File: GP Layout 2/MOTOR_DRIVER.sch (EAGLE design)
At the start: 52 parts, among them U3 MIC4604YM, U6 MIC4604YM, U7 ATMEGA328P_TQFP, Y1 16MHz

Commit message: checking that its updated
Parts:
- renumbered BOT_REVERSE to BOT_REV, TOP_REVERSE to TOP_REV, U3 to GATE1, U6 to GATE2
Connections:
- net BLT_RX: now also U$1.8; no longer U$1.7
- net BLT_TX: now also U$1.7; no longer U$1.8
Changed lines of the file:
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@@
 <parts>
 <part name="TOP_FWD" library="CSD18502KCS" deviceset="CSD18502KCS_KCS_3" device=""/>
-<part name="BOT_REVERSE" library="CSD18502KCS" deviceset="CSD18502KCS_KCS_3" device=""/>
+<part name="BOT_REV" library="CSD18502KCS" deviceset="CSD18502KCS_KCS_3" device=""/>
 <part name="FRAME1" library="frames" deviceset="A3L-LOC" device=""/>
-<part name="U3" library="MIC4604" deviceset="MIC4604YM" device=""/>
+<part name="GATE1" library="MIC4604" deviceset="MIC4604YM" device=""/>
 <part name="C1" library="resistor" deviceset="C-US" device="025-050X050" value="10uF"/>
 <part name="C2" library="resistor" deviceset="C-US" device="025-050X050" value="10uF"/>
 <part name="LSP3" library="solpad" deviceset="SE14" device=""/>
-<part name="TOP_REVERSE" library="CSD18502KCS" deviceset="CSD18502KCS_KCS_3" device=""/>
+<part name="TOP_REV" library="CSD18502KCS" deviceset="CSD18502KCS_KCS_3" device=""/>
 <part name="BOT_FWD" library="CSD18502KCS" deviceset="CSD18502KCS_KCS_3" device=""/>
-<part name="U6" library="MIC4604" deviceset="MIC4604YM" device=""/>
+<part name="GATE2" library="MIC4604" deviceset="MIC4604YM" device=""/>
 <part name="C3" library="resistor" deviceset="C-US" device="025-050X050" value="10uF"/>
 <part name="C4" library="resistor" deviceset="C-US" device="025-050X050" value="10uF"/>
@@
 <instances>
 <instance part="TOP_FWD" gate="A" x="124.46" y="210.82" rot="MR270"/>
-<instance part="BOT_REVERSE" gate="A" x="124.46" y="114.3" rot="MR270"/>
+<instance part="BOT_REV" gate="A" x="124.46" y="114.3" rot="MR270"/>
 <instance part="FRAME1" gate="G$1" x="0" y="0"/>
-<instance part="U3" gate="A" x="86.36" y="142.24" rot="MR0"/>
+<instance part="GATE1" gate="A" x="86.36" y="142.24" rot="MR0"/>
 <instance part="C1" gate="G$1" x="106.68" y="132.08" rot="R180"/>
 <instance part="C2" gate="G$1" x="116.84" y="132.08" rot="R180"/>
 <instance part="LSP3" gate="1" x="142.24" y="132.08" rot="R270"/>
-<instance part="TOP_REVERSE" gate="A" x="243.84" y="213.36" rot="R270"/>
+<instance part="TOP_REV" gate="A" x="243.84" y="213.36" rot="R270"/>
 <instance part="BOT_FWD" gate="A" x="243.84" y="114.3" rot="R270"/>
-<instance part="U6" gate="A" x="281.94" y="142.24"/>
+<instance part="GATE2" gate="A" x="281.94" y="142.24"/>
 <instance part="C3" gate="G$1" x="261.62" y="132.08" rot="MR180"/>
 <instance part="C4" gate="G$1" x="251.46" y="132.08" rot="MR180"/>
@@
 <net name="N$2" class="0">
 <segment>
-<pinref part="U3" gate="A" pin="LO"/>
+<pinref part="GATE1" gate="A" pin="LO"/>
 <wire x1="30.48" y1="142.24" x2="15.24" y2="142.24" width="0.1524" layer="91"/>
 <wire x1="15.24" y1="142.24" x2="15.24" y2="119.38" width="0.1524" layer="91"/>
-<pinref part="BOT_REVERSE" gate="A" pin="GATE"/>
+<pinref part="BOT_REV" gate="A" pin="GATE"/>
 <wire x1="15.24" y1="119.38" x2="124.46" y2="119.38" width="0.1524" layer="91"/>
 <wire x1="124.46" y1="119.38" x2="124.46" y2="114.3" width="0.1524" layer="91"/>
@@
 <wire x1="124.46" y1="218.44" x2="88.9" y2="218.44" width="0.1524" layer="91"/>
 <wire x1="88.9" y1="218.44" x2="88.9" y2="137.16" width="0.1524" layer="91"/>
-<pinref part="U3" gate="A" pin="HO"/>
+<pinref part="GATE1" gate="A" pin="HO"/>
 <wire x1="88.9" y1="137.16" x2="86.36" y2="137.16" width="0.1524" layer="91"/>
 </segment>
@@
 <net name="N$4" class="0">
 <segment>
-<pinref part="U3" gate="A" pin="HS"/>
+<pinref part="GATE1" gate="A" pin="HS"/>
 <wire x1="86.36" y1="134.62" x2="88.9" y2="134.62" width="0.1524" layer="91"/>
 <wire x1="88.9" y1="134.62" x2="88.9" y2="124.46" width="0.1524" layer="91"/>
@@
 <net name="N$5" class="0">
 <segment>
-<pinref part="U3" gate="A" pin="HB"/>
+<pinref part="GATE1" gate="A" pin="HB"/>
 <pinref part="C2" gate="G$1" pin="2"/>
 <wire x1="86.36" y1="139.7" x2="106.68" y2="139.7" width="0.1524" layer="91"/>
@@
 <net name="N$9" class="0">
 <segment>
-<pinref part="U6" gate="A" pin="LO"/>
+<pinref part="GATE2" gate="A" pin="LO"/>
 <wire x1="337.82" y1="142.24" x2="353.06" y2="142.24" width="0.1524" layer="91"/>
 <wire x1="353.06" y1="142.24" x2="353.06" y2="119.38" width="0.1524" layer="91"/>
@@
 <net name="N$10" class="0">
 <segment>
-<pinref part="TOP_REVERSE" gate="A" pin="GATE"/>
+<pinref part="TOP_REV" gate="A" pin="GATE"/>
 <wire x1="243.84" y1="213.36" x2="243.84" y2="218.44" width="0.1524" layer="91"/>
 <wire x1="243.84" y1="218.44" x2="279.4" y2="218.44" width="0.1524" layer="91"/>
 <wire x1="279.4" y1="218.44" x2="279.4" y2="137.16" width="0.1524" layer="91"/>
-<pinref part="U6" gate="A" pin="HO"/>
+<pinref part="GATE2" gate="A" pin="HO"/>
 <wire x1="279.4" y1="137.16" x2="281.94" y2="137.16" width="0.1524" layer="91"/>
 </segment>
@@
 <net name="N$11" class="0">
 <segment>
-<pinref part="U6" gate="A" pin="HS"/>
+<pinref part="GATE2" gate="A" pin="HS"/>
 <wire x1="281.94" y1="134.62" x2="279.4" y2="134.62" width="0.1524" layer="91"/>
 <wire x1="279.4" y1="134.62" x2="279.4" y2="124.46" width="0.1524" layer="91"/>
@@
 <net name="N$12" class="0">
 <segment>
-<pinref part="U6" gate="A" pin="HB"/>
+<pinref part="GATE2" gate="A" pin="HB"/>
 <pinref part="C4" gate="G$1" pin="2"/>
 <wire x1="281.94" y1="139.7" x2="261.62" y2="139.7" width="0.1524" layer="91"/>
@@
 <net name="LI2_TOP" class="0">
 <segment>
-<pinref part="U6" gate="A" pin="HI"/>
+<pinref part="GATE2" gate="A" pin="HI"/>
 <wire x1="337.82" y1="134.62" x2="350.52" y2="134.62" width="0.1524" layer="91"/>
 <label x="342.9" y="134.62" size="1.778" layer="95"/>
@@
 <net name="HI2_TOP" class="0">
 <segment>
-<pinref part="U6" gate="A" pin="LI"/>
+<pinref part="GATE2" gate="A" pin="LI"/>
 <wire x1="337.82" y1="137.16" x2="350.52" y2="137.16" width="0.1524" layer="91"/>
 <label x="342.9" y="137.16" size="1.778" layer="95"/>
@@
 <net name="GND_TOP" class="0">
 <segment>
-<pinref part="BOT_REVERSE" gate="A" pin="SOURCE"/>
+<pinref part="BOT_REV" gate="A" pin="SOURCE"/>
 <wire x1="127" y1="48.26" x2="127" y2="40.64" width="0.1524" layer="91"/>
-<pinref part="U3" gate="A" pin="VSS"/>
+<pinref part="GATE1" gate="A" pin="VSS"/>
 <wire x1="30.48" y1="139.7" x2="12.7" y2="139.7" width="0.1524" layer="91"/>
 <wire x1="12.7" y1="139.7" x2="12.7" y2="40.64" width="0.1524" layer="91"/>
@@
 <pinref part="BOT_FWD" gate="A" pin="SOURCE"/>
 <wire x1="241.3" y1="48.26" x2="241.3" y2="40.64" width="0.1524" layer="91"/>
-<pinref part="U6" gate="A" pin="VSS"/>
+<pinref part="GATE2" gate="A" pin="VSS"/>
 <wire x1="337.82" y1="139.7" x2="355.6" y2="139.7" width="0.1524" layer="91"/>
 <wire x1="355.6" y1="139.7" x2="355.6" y2="40.64" width="0.1524" layer="91"/>
@@
 <wire x1="86.36" y1="220.98" x2="86.36" y2="147.32" width="0.1524" layer="91"/>
 <junction x="127" y="220.98"/>
-<pinref part="U3" gate="A" pin="VDD"/>
-<pinref part="TOP_REVERSE" gate="A" pin="DRAIN"/>
+<pinref part="GATE1" gate="A" pin="VDD"/>
+<pinref part="TOP_REV" gate="A" pin="DRAIN"/>
 <wire x1="86.36" y1="147.32" x2="86.36" y2="142.24" width="0.1524" layer="91"/>
 <wire x1="241.3" y1="220.98" x2="241.3" y2="213.36" width="0.1524" layer="91"/>
 <wire x1="241.3" y1="220.98" x2="281.94" y2="220.98" width="0.1524" layer="91"/>
 <wire x1="281.94" y1="220.98" x2="281.94" y2="147.32" width="0.1524" layer="91"/>
-<pinref part="U6" gate="A" pin="VDD"/>
+<pinref part="GATE2" gate="A" pin="VDD"/>
 <wire x1="281.94" y1="147.32" x2="281.94" y2="142.24" width="0.1524" layer="91"/>
 <wire x1="127" y1="220.98" x2="175.26" y2="220.98" width="0.1524" layer="91"/>
@@
 <segment>
 <pinref part="TOP_FWD" gate="A" pin="SOURCE"/>
-<pinref part="BOT_REVERSE" gate="A" pin="DRAIN"/>
+<pinref part="BOT_REV" gate="A" pin="DRAIN"/>
 <wire x1="127" y1="144.78" x2="127" y2="132.08" width="0.1524" layer="91"/>
 <pinref part="LSP3" gate="1" pin="MP"/>
@@
 <net name="MOTOR_LOW_TOP" class="0">
 <segment>
-<pinref part="TOP_REVERSE" gate="A" pin="SOURCE"/>
+<pinref part="TOP_REV" gate="A" pin="SOURCE"/>
 <pinref part="BOT_FWD" gate="A" pin="DRAIN"/>
 <wire x1="241.3" y1="147.32" x2="241.3" y2="132.08" width="0.1524" layer="91"/>
@@
 <net name="LI1_TOP" class="0">
 <segment>
-<pinref part="U3" gate="A" pin="LI"/>
+<pinref part="GATE1" gate="A" pin="LI"/>
 <wire x1="30.48" y1="137.16" x2="20.32" y2="137.16" width="0.1524" layer="91"/>
 <label x="20.32" y="137.16" size="1.778" layer="95"/>
@@
 <net name="HI1_TOP" class="0">
 <segment>
-<pinref part="U3" gate="A" pin="HI"/>
+<pinref part="GATE1" gate="A" pin="HI"/>
 <wire x1="30.48" y1="134.62" x2="20.32" y2="134.62" width="0.1524" layer="91"/>
 <label x="20.32" y="134.62" size="1.778" layer="95"/>
@@
 </segment>
 </net>
-<net name="BLT_RX" class="0">
+<net name="BLT_TX" class="0">
 <segment>
 <wire x1="238.76" y1="147.32" x2="223.52" y2="147.32" width="0.1524" layer="91"/>
 <label x="223.52" y="147.32" size="1.778" layer="95"/>
 <pinref part="U$1" gate="G$1" pin="7"/>
-</segment>
-</net>
-<net name="BLT_TX" class="0">
-<segment>
-<wire x1="238.76" y1="144.78" x2="223.52" y2="144.78" width="0.1524" layer="91"/>
-<label x="223.52" y="144.78" size="1.778" layer="95"/>
-<pinref part="U$1" gate="G$1" pin="8"/>
 </segment>
 </net>
@@
 </segment>
 </net>
+<net name="BLT_RX" class="0">
+<segment>
+<wire x1="238.76" y1="144.78" x2="223.52" y2="144.78" width="0.1524" layer="91"/>
+<label x="223.52" y="144.78" size="1.778" layer="95"/>
+<pinref part="U$1" gate="G$1" pin="8"/>
+</segment>
+</net>

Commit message: added gpio, modified layout
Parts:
- added MOTOR_NEG_B: SE14, solpad:SE14
- added TGPIO: (no value), con-lsta:FE09-1
- renumbered LSP3 to MOTOR_POS, LSP4 to BATT_HIGH, LSP5 to BATT_LOW, LSP6 to MOTOR_NEG
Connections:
- removed net M1_GPIO4: U7.PD3(INT1)
- new net LED1: U$1.14/A0
- new net LED2: U$1.15/A1
- new net LED3: U$1.16/A2
- new net TGPIO1: TGPIO.1, U$1.33/A14
- new net TGPIO2: TGPIO.2, U$1.34/A15
- new net TGPIO3: TGPIO.3, U$1.35/A16
- new net TGPIO4: TGPIO.4, U$1.36/A17
- new net TGPIO5: TGPIO.5, U$1.37/A18
- new net TGPIO6: TGPIO.6, U$1.38/A19
- new net TGPIO7: TGPIO.7, U$1.39/A20
- new net TGPIO8: TGPIO.8, U$1.A21/DAC0
- new net TGPIO9: TGPIO.9, U$1.A22/DAC1
- net BATT_VOLTAGE_SENSE: now also U$1.17/A3; no longer U$1.14/A0
- net EMF_SENSE_HIGH: now also U$1.19/A5/SCL; no longer U$1.17/A3
- net EMF_SENSE_LOW: now also U$1.18/A4/SDA; no longer U$1.16/A2
- net GND_TOP: now also MOTOR_NEG_B.MP
- net HALL1_B: now also U$1.1/TX; no longer U$1.39/A20
- net HALL2: now also U7.PD3(INT1)
- net HALL2_B: now also U$1.2; no longer U$1.38/A19
- net REC_EXTRA1: now also U$1.22/A8
- net REC_EXTRA2: now also U$1.23/A9
- net REC_MOTOR: now also REC.4, U$1.21/A7; no longer REC.3, U$1.15/A1
- net REC_SERVO: now also REC.3, U$1.20/A6; no longer REC.4, U$1.18/A4/SDA
- net SERVO: now also U$1.9/CS; no longer U$1.20/A6

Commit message: ISCP connectors
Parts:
- removed TXRX: (no value), con-lsta:FE02-1
- added PROGRAM: (no value), arduino_jw:ARDUINO_CONN-ICSP
- R1: value 9090 -> 2800
- R2: value 4750 -> 1620
- R3: value 2.32M -> 2320
- R4: value 1.15M -> 1150
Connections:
- net RX: no longer TXRX.1
- net TX: no longer TXRX.2
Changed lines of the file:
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@@
 <part name="FUSE" library="minifuse" deviceset="FUSEHOLDER3588" device=""/>
 <part name="BIG_SWITCH" library="bigswitch" deviceset="BIGSWITCH" device=""/>
-<part name="R1" library="SparkFun-Resistors" deviceset="0.3OHM" device="-0805-1/8W-1%" value="9090"/>
-<part name="R2" library="SparkFun-Resistors" deviceset="0.3OHM" device="-0805-1/8W-1%" value="4750"/>
+<part name="R1" library="SparkFun-Resistors" deviceset="0.3OHM" device="-0805-1/8W-1%" value="2800"/>
+<part name="R2" library="SparkFun-Resistors" deviceset="0.3OHM" device="-0805-1/8W-1%" value="1620"/>
 <part name="SUPPLY2" library="supply2" deviceset="GND" device=""/>
-<part name="R3" library="SparkFun-Resistors" deviceset="0.3OHM" device="-0805-1/8W-1%" value="2.32M"/>
-<part name="R4" library="SparkFun-Resistors" deviceset="0.3OHM" device="-0805-1/8W-1%" value="1.15M"/>
+<part name="R3" library="SparkFun-Resistors" deviceset="0.3OHM" device="-0805-1/8W-1%" value="2320"/>
+<part name="R4" library="SparkFun-Resistors" deviceset="0.3OHM" device="-0805-1/8W-1%" value="1150"/>
 <part name="U$2" library="heatsink" deviceset="HEATSINK" device=""/>
 <part name="U$4" library="heatsink" deviceset="HEATSINK" device=""/>
@@
 <part name="HALL1_B" library="con-lstb" deviceset="MA03-1" device=""/>
 <part name="HALL2_B" library="con-lstb" deviceset="MA03-1" device=""/>
-<part name="TXRX" library="con-lsta" deviceset="FE02-1" device=""/>
 <part name="MOTOR_NEG_B" library="solpad" deviceset="SE14" device=""/>
 <part name="TGPIO" library="con-lsta" deviceset="FE09-1" device=""/>
+<part name="PROGRAM" library="arduino_jw" deviceset="ARDUINO_CONN-ICSP" device=""/>
 </parts>
 <sheets>
@@
 <instance part="HALL1_B" gate="G$1" x="304.8" y="104.14"/>
 <instance part="HALL2_B" gate="G$1" x="304.8" y="86.36"/>
-<instance part="TXRX" gate="G$1" x="208.28" y="71.12"/>
 <instance part="TGPIO" gate="G$1" x="121.92" y="68.58"/>
+<instance part="PROGRAM" gate="G$1" x="236.22" y="60.96"/>
 </instances>
 <busses>
@@
 </segment>
 </net>
-<net name="TX" class="0">
-<segment>
-<pinref part="TXRX" gate="G$1" pin="2"/>
-<wire x1="215.9" y1="71.12" x2="226.06" y2="71.12" width="0.1524" layer="91"/>
-<label x="220.98" y="71.12" size="1.778" layer="95"/>
-</segment>
-</net>
-<net name="RX" class="0">
-<segment>
-<pinref part="TXRX" gate="G$1" pin="1"/>
-<wire x1="215.9" y1="68.58" x2="226.06" y2="68.58" width="0.1524" layer="91"/>
-<label x="220.98" y="68.58" size="1.778" layer="95"/>
-</segment>
-</net>

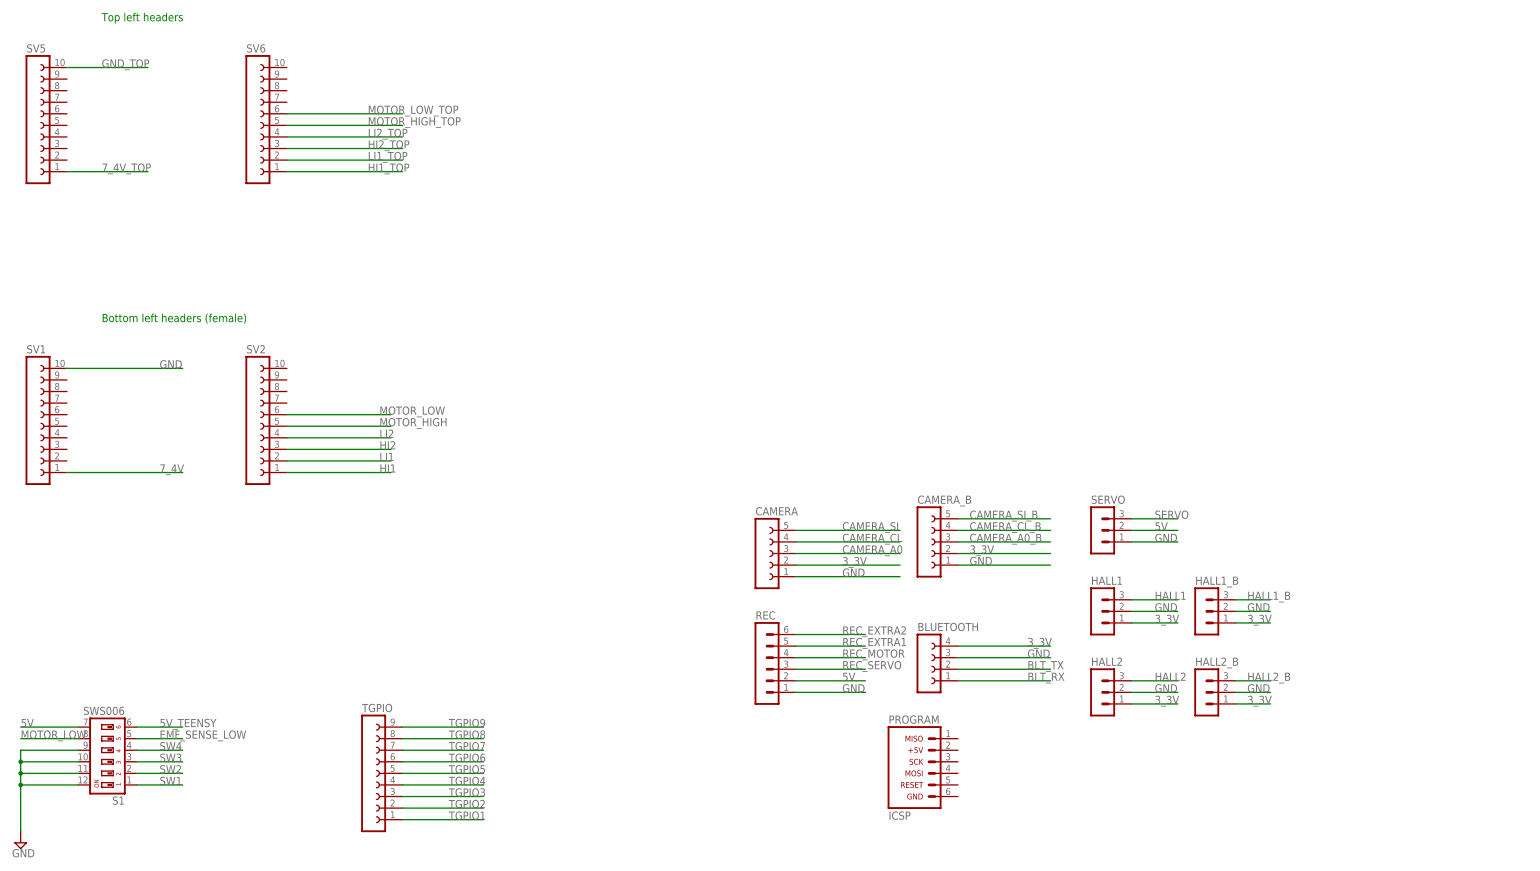
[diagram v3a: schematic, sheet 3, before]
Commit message: added led driver, indicator leds, etc
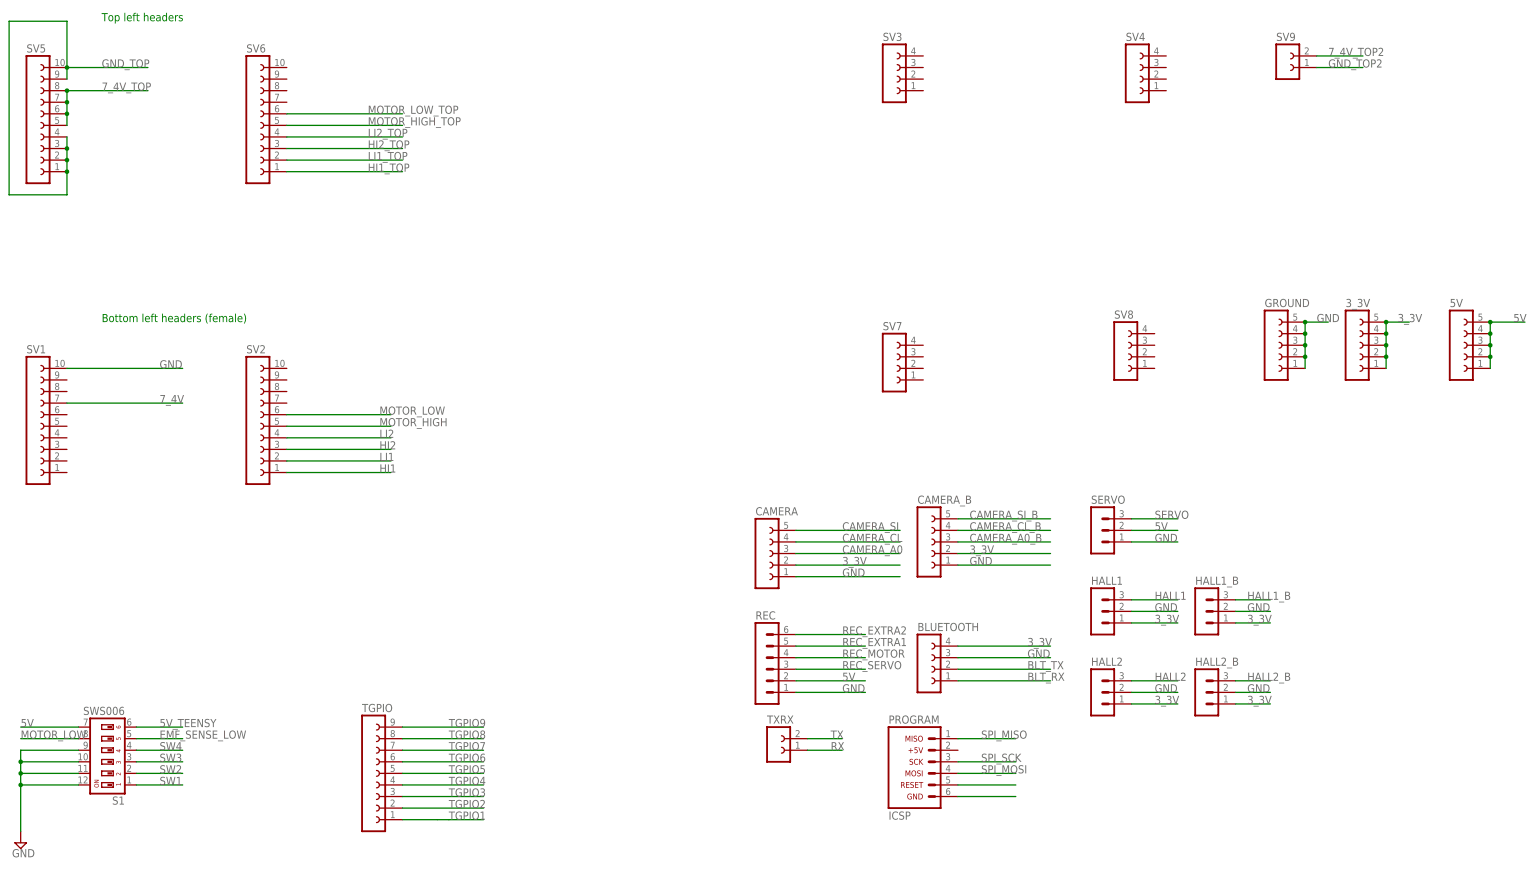
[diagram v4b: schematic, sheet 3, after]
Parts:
- added 3_3V, 5V, GROUND: (no value), con-lsta:FE05-1
- added D1, D2, D5: (no value), SparkFun-LED:LED0603
- added LED1, LED2, SV9, TXRX: (no value), con-lsta:FE02-1
- added LED_DRIVER1, LED_DRIVER2: CSD18502KCS_KCS_3, CSD18502KCS:CSD18502KCS_KCS_3
- added R10, R11, R9: (no value), rcl:R-US_R0805
- added R5, R7: (no value), rcl:R-US_R2512
- added R6, R8: 1k, SparkFun-Resistors:1KOHM-HORIZ-1/4W-1%
- added SV3, SV4, SV7, SV8: (no value), con-lsta:FE04-1
- added T1, T2: 2N2222, transistor:2N2222
- added U$3, U$7: POT, ledpot:POT
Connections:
- net N$13 renamed SPI_SS
- new net 7_4V_TOP2: LED1.2, LED2.2, R6.2, R8.2, SV9.2
- new net GND_TOP2: SV9.1, T1.E, T2.E, U$3.P2, U$7.P2
- new net N$1: R5.1, U$7.P3
- new net N$13: R7.1, U$3.P3
- new net N$14: PROGRAM.5
- new net N$17: LED1.1, LED_DRIVER2.DRAIN
- new net N$19: LED_DRIVER1.GATE, R8.1, T2.C
- new net N$20: LED2.1, LED_DRIVER1.DRAIN
- new net N$22: D1.A, R9.1
- new net N$23: D2.A, R10.1
- new net N$24: D5.A, R11.1
- new net N$8: LED_DRIVER2.SOURCE, R5.2, T1.B
- new net SPI_MISO: PROGRAM.1, U$1.11/MOSI, U7.PB4(MISO)
- new net SPI_MOSI: PROGRAM.4, U$1.12/MISO, U7.PB3(MOSI/OC2)
- new net SPI_SCK: PROGRAM.3, U$1.13/SCK, U7.PB5(SCK)
- net 3_3V: now also 3_3V.1, 3_3V.2, 3_3V.3, 3_3V.4, 3_3V.5
- net 5V: now also 5V.1, 5V.2, 5V.3, 5V.4, 5V.5
- net 7_4V: now also SV1.7; no longer SV1.1
- net 7_4V_TOP: now also SV5.5, SV5.6, SV5.7, SV5.8; no longer SV5.1
- net GND: now also D1.C, D2.C, D5.C, GROUND.1, GROUND.2, GROUND.3, GROUND.4, GROUND.5
- net GND_TOP: now also SV5.1, SV5.2, SV5.3, SV5.4, SV5.9
- net LED1: now also R9.2
- net LED2: now also R10.2
- net LED3: now also R11.2
- net N$15: now also PROGRAM.6; no longer U$1.12/MISO, U7.PB3(MOSI/OC2)
- net N$16: now also LED_DRIVER2.GATE, R6.1, T1.C; no longer U$1.13/SCK, U7.PB5(SCK)
- net N$18: now also LED_DRIVER1.SOURCE, R7.2, T2.B; no longer U$1.11/MOSI, U7.PB4(MISO)
- net RX: now also TXRX.1
- net TX: now also TXRX.2
